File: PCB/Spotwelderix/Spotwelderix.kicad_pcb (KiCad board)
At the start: 2 copper layers, 128.5 x 64.2 mm, 41 parts, among them IC1 IXDD604SIA, IC2 IXDD604SIA, IC3 IXDD604SIA, J4 probe-, P1 CONN_01X08, Q1 IRFB7430, Q2 IRFB7430, Q3 IRFB7430, Q4 IRFB7430, Q5 IRFB7430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

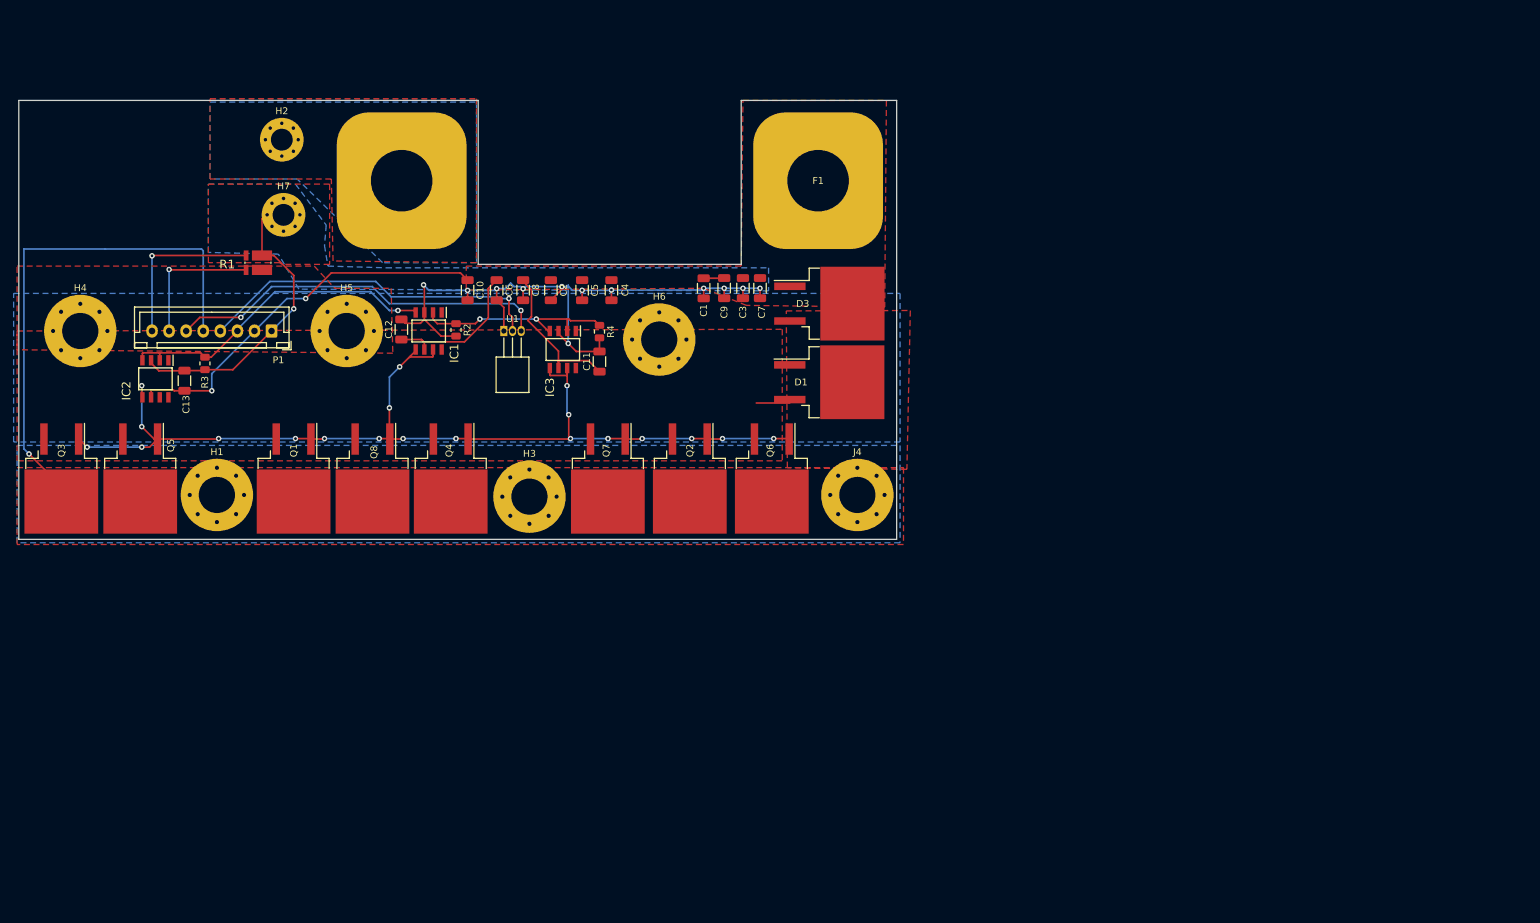
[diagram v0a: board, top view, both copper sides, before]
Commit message: power pcb updated, added safe power for driver
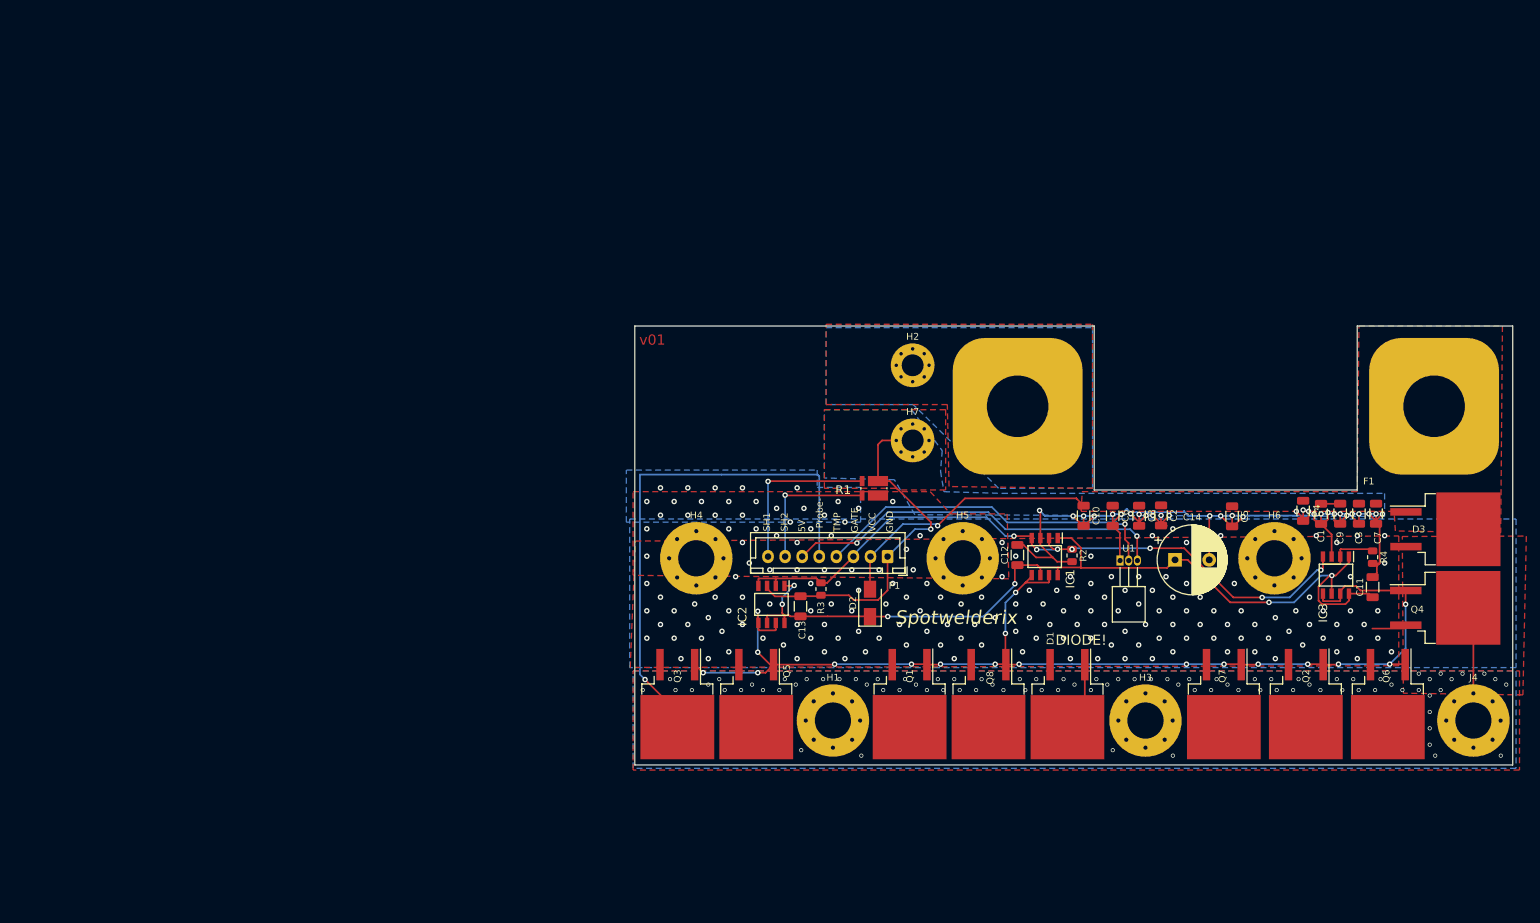
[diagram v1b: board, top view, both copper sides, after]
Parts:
- added C14: 470µ, Capacitor_THT:CP_Radial_D10.0mm_P5.00mm, F.Cu at (155.2, 99.5)
- added D2: D, Diode_SMD:D_SMA, F.Cu at (110.6, 105.8)
- moved Q4 146.8 mm to (194.8, 106.5), turned to 0 degrees
- moved IC3 117.9 mm to (178.8, 101.7)
- moved C11 117.9 mm to (184.2, 103.5)
- moved R4 117.9 mm to (184.2, 99.1)
- moved C4 106.3 mm to (174.0, 92.3)
- moved C5 100.7 mm to (163.6, 93.1)
- moved H2 98.1 mm to (116.8, 71.0)
- moved H7 97.8 mm to (116.8, 82.0)
- moved U1 96.3 mm to (147.2, 99.6)
- moved C1 96.2 mm to (176.6, 92.8)
- moved H4 96.1 mm to (85.2, 99.3)
- moved H5 96.1 mm to (124.2, 99.3)
- moved C6 96.0 mm to (146.1, 93.0)
- moved C8 96.0 mm to (150.0, 93.0)
- moved D3 96.0 mm to (194.8, 95.0)
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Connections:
- C1 pad 1: VCC -> VCCQ
- C10 pad 1: VCC -> VCCQ
- C2 pad 1: VCC -> VCCQ
- C3 pad 1: VCC -> VCCQ
- C4 pad 1: VCC -> VCCQ
- C5 pad 1: VCC -> VCCQ
- C6 pad 1: VCC -> VCCQ
- C7 pad 1: VCC -> VCCQ
- C8 pad 1: VCC -> VCCQ
- C9 pad 1: VCC -> VCCQ
- D3 pad 1: VCC -> VCCQ
- F1 pad 1: VCC -> VCCQ
- IC1 pad 1: Net-(IC1-Pad1) -> VCC
- IC1 pad 8: Net-(IC1-Pad8) -> VCC
- IC2 pad 1: Net-(IC2-Pad1) -> VCC
- IC2 pad 8: Net-(IC2-Pad8) -> VCC
- IC3 pad 1: Net-(IC3-Pad1) -> VCC
- IC3 pad 8: Net-(IC3-Pad8) -> VCC
- P1 pad 2: VCC -> VCCQ
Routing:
- net GND: track 149.8 -> 197.9 mm, vias 13 -> 31
- net VCCQ: track 0.00 -> 43.2 mm, vias 0 -> 1
- net Gate_logic: track 78.5 -> 110.8 mm, vias 3 -> 7
- net VCC: track 105.0 -> 132.3 mm, vias 2 -> 6
- net Probe-: track 77.3 -> 104.4 mm, vias 1 -> 90
- net Gate: track 150.5 -> 166.9 mm, vias 20 -> 18
- net FET_GND: vias 0 -> 185
- added copper zone on F.Cu, net VCCQ
- removed copper zone on F.Cu, net VCC
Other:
- board size 128.5 x 64.2 mm -> 128.5 x 64.3 mm
- board text added: "5V"
- board text added: "DIODE!"
- board text added: "GATE"
- board text added: "GND"
- board text added: "Probe-"
- board text added: "SH1"
- board text added: "SH2"
- board text added: "Spotwelderix"
- board text added: "TMP"
- board text added: "VCC"
- board text added: "v01"

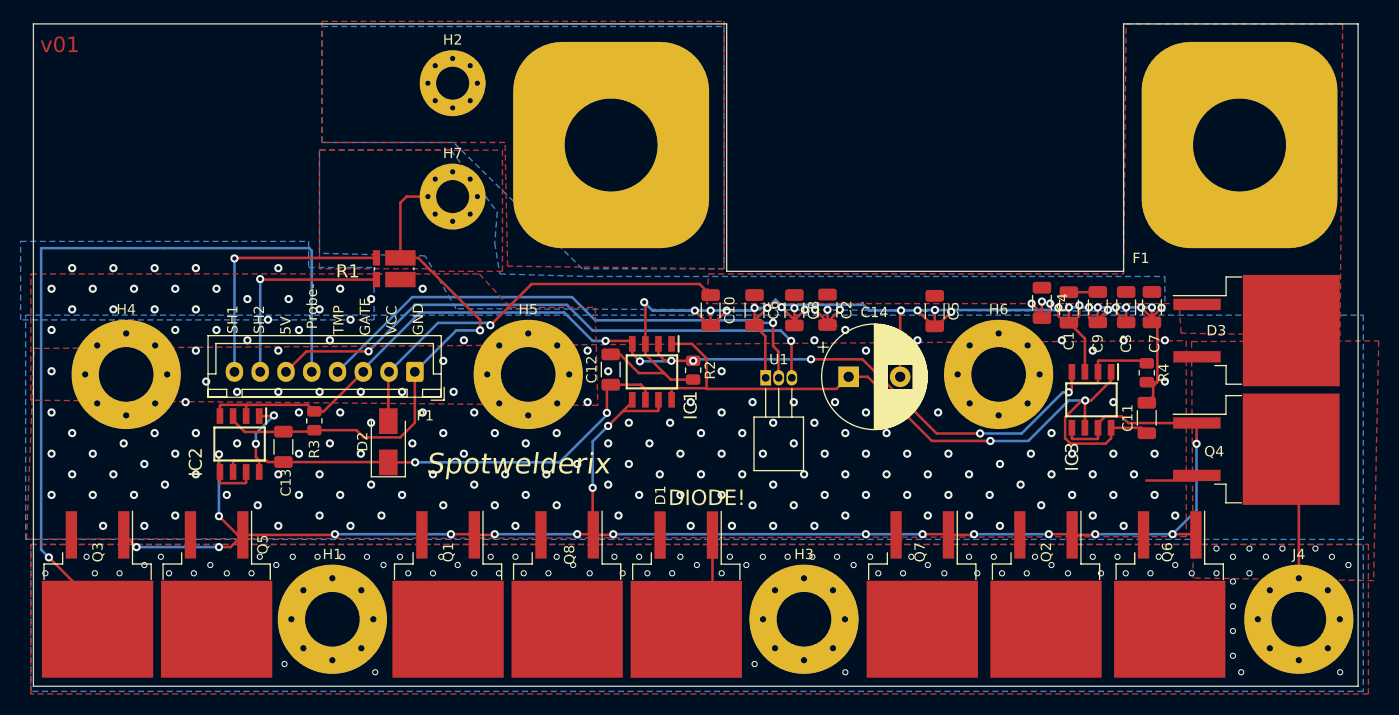
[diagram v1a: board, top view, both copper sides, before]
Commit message: ena powerpcb added
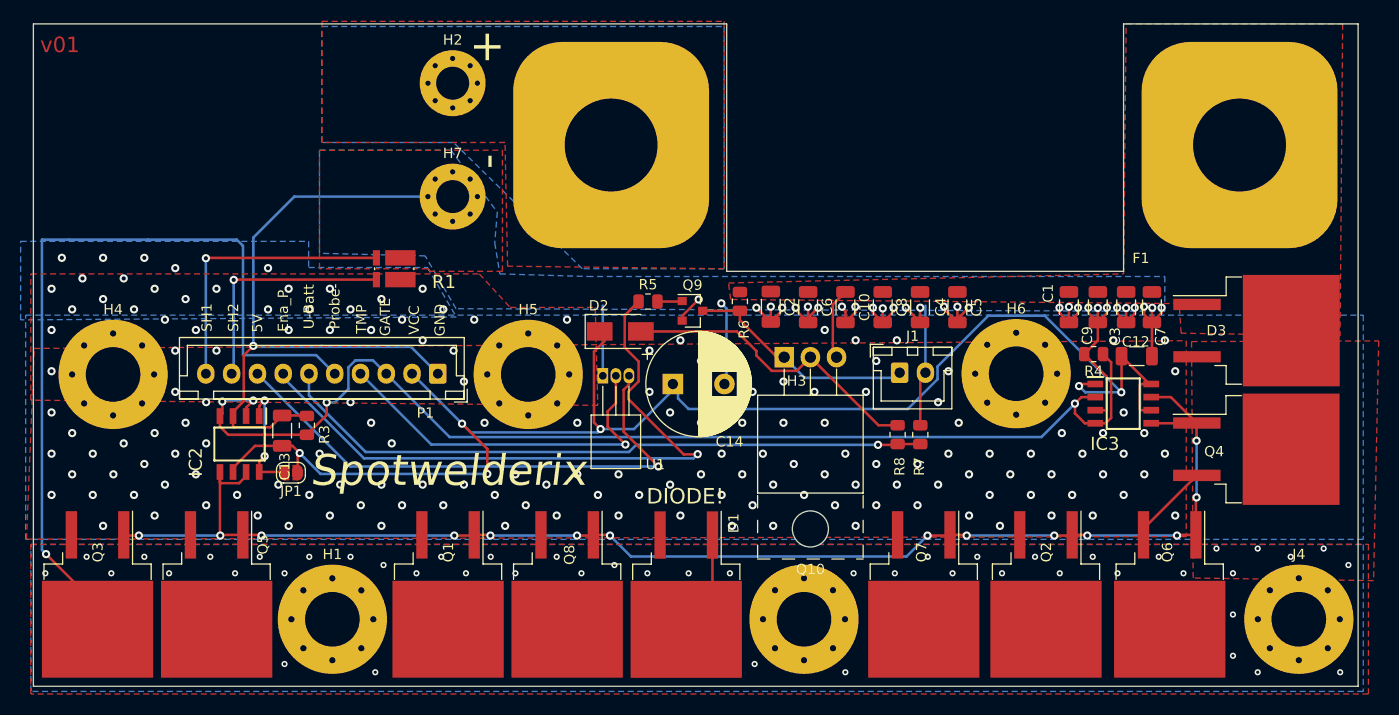
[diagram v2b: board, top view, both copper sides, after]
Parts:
- removed C11: 10µ, Capacitor_SMD:C_1206_3216Metric
- removed IC1: IXDD604SIA, SamacSys_Parts:SOIC127P600X175-8N
- removed R2: 10k, Resistor_SMD:R_0805_2012Metric
- added J1: OnOffTast, Connector_JST:JST_XH_B2B-XH-A_1x02_P2.50mm_Vertical, F.Cu at (160.2, 99.1)
- added JP1: Jumper_NO_Small, Jumper:SolderJumper-2_P1.3mm_Open_RoundedPad1.0x1.5mm, F.Cu at (101.2, 108.8)
- added Q10: FQP27P06, Package_TO_SOT_THT:TO-220-3_Horizontal_TabUp, F.Cu at (149.0, 97.6)
- added Q9: BC807, Package_TO_SOT_SMD:SOT-23, F.Cu at (140.1, 93.1)
- added R5: 22k, Resistor_SMD:R_0805_2012Metric, F.Cu at (135.8, 92.2)
- added R6: 22k, Resistor_SMD:R_0805_2012Metric, F.Cu at (144.7, 92.2)
- added R7: 33k, Resistor_SMD:R_0805_2012Metric, F.Cu at (160.0, 105.1)
- added R8: 10k, Resistor_SMD:R_0805_2012Metric, F.Cu at (162.2, 105.1)
- P1: value CONN_01X08 -> CONN_01X09; footprint Connector_JST:JST_XH_B8B-XH-A_1x08_P2.50mm_Vertical -> Connector_JST:JST_XH_B10B-XH-A_1x10_P2.50mm_Vertical
- moved C12 51.0 mm to (183.2, 97.5), turned to 0 degrees
- moved D2 24.9 mm to (133.1, 95.1), turned to 0 degrees
- moved C14 17.1 mm to (138.2, 100.2)
- moved U1 15.8 mm to (131.4, 99.4)
- moved C10 13.1 mm to (154.9, 92.7)
- moved C4 11.8 mm to (162.2, 92.7)
- moved C8 8.58 mm to (158.6, 92.7)
- moved C2 5.51 mm to (147.7, 92.7)
- moved R4 5.47 mm to (179.0, 97.3), turned to 180 degrees
- moved C6 5.21 mm to (151.3, 92.7)
- moved IC3 3.11 mm to (181.9, 102.1), turned to 0 degrees
- moved P1 2.24 mm to (115.4, 99.2)
- moved C5 2.23 mm to (165.8, 92.7)
- moved H6 1.70 mm to (171.5, 99.2)
- moved C13 1.57 mm to (100.3, 104.7)
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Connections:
- D2 pad 2: VCCQ -> Net-(D2-Pad2)
- IC2 pad 1: VCC -> Net-(IC2-Pad1)
- IC2 pad 8: VCC -> Net-(IC2-Pad1)
- P1 pad 2: VCCQ -> VCC
- P1 pad 6: +5V -> V_Batt
- P1 pad 7: R_Schunt_H -> EnablePower
- P1 pad 8: R_Schunt_L -> +5V
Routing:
- net EnablePower: track 0.00 -> 64.1 mm, vias 0 -> 1
- net V_Batt: track 0.00 -> 64.0 mm, vias 0 -> 1
- net GND: track 197.9 -> 159.1 mm
- net VCCQ: track 43.2 -> 7.55 mm, vias 1 -> 0
- net Net-(D2-Pad2): track 0.00 -> 30.0 mm
- net Gate: track 166.9 -> 137.2 mm, vias 18 -> 14
- net Net-(J1-Pad1): track 0.00 -> 22.5 mm
- net Dallas: track 51.3 -> 36.3 mm
- net Probe-: track 104.4 -> 90.2 mm, vias 90 -> 50
- net VCC: track 132.3 -> 144.7 mm
- net Net-(IC2-Pad1): track 0.00 -> 11.3 mm, vias 0 -> 2
- net +5V: track 56.2 -> 53.0 mm, vias 2 -> 1
- net FET_GND: track 4.89 -> 7.91 mm, vias 185 -> 162
- net Gate_logic: track 110.8 -> 113.8 mm, vias 7 -> 4
- net R_Schunt_L: track 24.8 -> 27.8 mm
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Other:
- board text added: "+"
- board text added: "-"
- board text added: "Ena_P"
- board text added: "U-Batt"

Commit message: shunt replace
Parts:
- added IC1: INA213AIDCKR, SamacSys_Parts:SOT65P210X110-6N, F.Cu at (101.8, 86.5)
- added R10: 30, Resistor_SMD:R_0805_2012Metric, F.Cu at (97.7, 87.8)
- added R11: 30k, Resistor_SMD:R_0805_2012Metric, F.Cu at (106.9, 85.1)
- added R12: 30k, Resistor_SMD:R_0805_2012Metric, F.Cu at (110.3, 83.7)
- added R2: 10k, Resistor_SMD:R_0805_2012Metric, F.Cu at (132.1, 91.1)
- added R9: 100, Resistor_SMD:R_0805_2012Metric, F.Cu at (97.6, 90.2)
- added U2: LM4040DBZ-2.0, Package_TO_SOT_SMD:SOT-23, F.Cu at (93.7, 89.1)
- P1: footprint Connector_JST:JST_XH_B10B-XH-A_1x10_P2.50mm_Vertical -> Connector_JST:JST_XH_B9B-XH-A_1x09_P2.50mm_Vertical
- Q9: value BC807 -> BC817
- R1: value R_Shunt -> 100µ; footprint SamacSys_Parts:WSK12161L000FEA -> Resistor_SMD:R_Shunt_Vishay_WSR2_WSR3
- moved R1 1.23 mm to (112.3, 89.5), turned to 0 degrees
- moved Q9 1.01 mm to (140.6, 92.2), turned to 270 degrees
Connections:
- P1 pad 9: R_Schunt_H -> R_Schunt_Stab
- R1 pad 1: GND -> FET_GND
- R1 pad 2: R_Schunt_L -> GND
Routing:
- net R_Schunt_L: track 27.8 -> 0.00 mm, vias 1 -> 0
- net GND: track 159.1 -> 186.2 mm, vias 31 -> 33
- net R_Schunt_Stab: track 0.00 -> 24.4 mm, vias 0 -> 1
- net R_Schunt_H: track 23.0 -> 0.00 mm, vias 1 -> 0
- net +5V: track 53.0 -> 71.8 mm, vias 1 -> 2
- net Net-(IC1-Pad5): track 0.00 -> 8.96 mm
- net Net-(IC1-Pad1): track 0.00 -> 7.97 mm
- net FET_GND: track 7.91 -> 15.4 mm, vias 162 -> 157
- net Net-(Q9-Pad1): track 2.42 -> 9.42 mm
- net Net-(IC1-Pad4): track 0.00 -> 3.69 mm
- net Gate: track 137.2 -> 140.3 mm, vias 14 -> 15
- net Net-(J1-Pad1): track 22.5 -> 23.1 mm
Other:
- board text added: "v01123"
- board text removed: "v01"

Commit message: ordered seperately
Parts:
- moved R11 0.40 mm to (106.9, 84.7)
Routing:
- net GND: track 186.2 -> 186.9 mm
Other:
- outline, holes or cut-outs redrawn

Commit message: pcb update 1.9
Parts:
- removed R10: 30, Resistor_SMD:R_0805_2012Metric
- removed R9: 100, Resistor_SMD:R_0805_2012Metric
- added C11: 100n, Capacitor_SMD:C_0805_2012Metric_Pad1.18x1.45mm_HandSolder, F.Cu at (98.4, 88.8)
- Q10: footprint Package_TO_SOT_THT:TO-220-3_Horizontal_TabUp -> Package_TO_SOT_THT:TO-220-3_Horizontal_TabDown
- R8: value 10k -> 6.5k
- U2: value LM4040DBZ-2.0 -> REF3020
- moved Q10 5.02 mm to (154.0, 97.2), turned to 180 degrees
- moved U2 0.86 mm to (94.4, 88.6)
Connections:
- IC1 pad 1: Net-(IC1-Pad1) -> Net-(C11-Pad1)
- U2 pad 1: Net-(IC1-Pad1) -> +5V
- U2 pad 2: GND -> Net-(C11-Pad1)
- U2 pad 3: (no net) -> GND
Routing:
- net Net-(IC1-Pad1): track 7.97 -> 0.00 mm
- net Net-(C11-Pad1): track 0.00 -> 7.64 mm
- net VCCQ: track 7.55 -> 10.1 mm
- net GND: track 186.9 -> 189.1 mm
- net +5V: track 71.8 -> 73.0 mm
- net Net-(J1-Pad1): track 23.1 -> 23.5 mm, vias 0 -> 1
- net FET_GND: vias 157 -> 156
- net (no net): vias 0 -> 1
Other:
- board text added: "v02"
- board text removed: "v01123"
